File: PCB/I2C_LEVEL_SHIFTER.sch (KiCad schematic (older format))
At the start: 6 parts

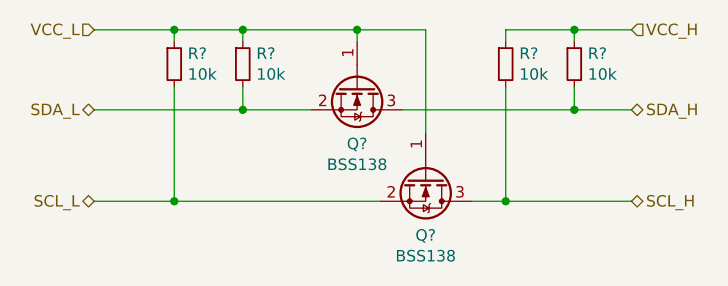
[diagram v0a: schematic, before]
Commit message: Added Humidity and temperature sensors
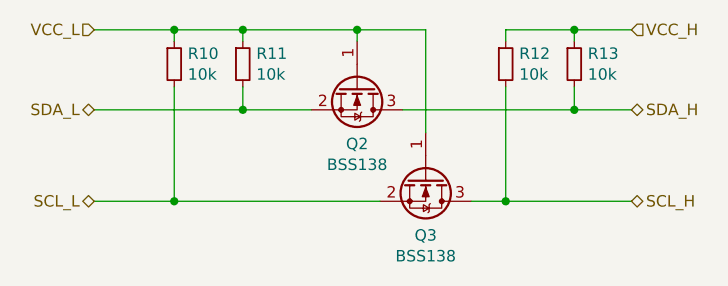
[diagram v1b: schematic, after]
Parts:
- gave numbers to parts that had none: 6
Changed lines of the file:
@@
 $EndDescr
 $Comp
-L Transistor_FET:BSS138 Q?
+L Transistor_FET:BSS138 Q2
 U 1 1 5E8E373A
 P 6100 3750
-F 0 "Q?" V 6349 3750 50  0000 C CNN
+F 0 "Q2" V 6349 3750 50  0000 C CNN
 F 1 "BSS138" V 6440 3750 50  0000 C CNN
 F 2 "Package_TO_SOT_SMD:SOT-23" H 6300 3675 50  0001 L CIN
@@
 $EndComp
 $Comp
-L Transistor_FET:BSS138 Q?
+L Transistor_FET:BSS138 Q3
 U 1 1 5E8E4A70
 P 6400 4150
-F 0 "Q?" V 6649 4150 50  0000 C CNN
+F 0 "Q3" V 6649 4150 50  0000 C CNN
 F 1 "BSS138" V 6740 4150 50  0000 C CNN
 F 2 "Package_TO_SOT_SMD:SOT-23" H 6600 4075 50  0001 L CIN
@@
 	6300 3850 7050 3850
 $Comp
-L Device:R_Small R?
+L Device:R_Small R13
 U 1 1 5E8E9A65
 P 7050 3650
-F 0 "R?" H 7109 3696 50  0000 L CNN
+F 0 "R13" H 7109 3696 50  0000 L CNN
 F 1 "10k" H 7109 3605 50  0000 L CNN
 F 2 "" H 7050 3650 50  0001 C CNN
@@
 $EndComp
 $Comp
-L Device:R_Small R?
+L Device:R_Small R12
 U 1 1 5E8EA22E
 P 6750 3650
-F 0 "R?" H 6809 3696 50  0000 L CNN
+F 0 "R12" H 6809 3696 50  0000 L CNN
 F 1 "10k" H 6809 3605 50  0000 L CNN
 F 2 "" H 6750 3650 50  0001 C CNN
@@
 $EndComp
 $Comp
-L Device:R_Small R?
+L Device:R_Small R11
 U 1 1 5E8EC794
 P 5600 3650
-F 0 "R?" H 5659 3696 50  0000 L CNN
+F 0 "R11" H 5659 3696 50  0000 L CNN
 F 1 "10k" H 5659 3605 50  0000 L CNN
 F 2 "" H 5600 3650 50  0001 C CNN
@@
 $EndComp
 $Comp
-L Device:R_Small R?
+L Device:R_Small R10
 U 1 1 5E8EC79A
 P 5300 3650
-F 0 "R?" H 5359 3696 50  0000 L CNN
+F 0 "R10" H 5359 3696 50  0000 L CNN
 F 1 "10k" H 5359 3605 50  0000 L CNN
 F 2 "" H 5300 3650 50  0001 C CNN

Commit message: Added majority footprints
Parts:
- R10, R11, R12, R13: footprint (none) -> Resistor_SMD:R_0603_1608Metric
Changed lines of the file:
@@
 F 0 "R13" H 7109 3696 50  0000 L CNN
 F 1 "10k" H 7109 3605 50  0000 L CNN
-F 2 "" H 7050 3650 50  0001 C CNN
+F 2 "Resistor_SMD:R_0603_1608Metric" H 7050 3650 50  0001 C CNN
 F 3 "~" H 7050 3650 50  0001 C CNN
 	1    7050 3650
@@
 F 0 "R12" H 6809 3696 50  0000 L CNN
 F 1 "10k" H 6809 3605 50  0000 L CNN
-F 2 "" H 6750 3650 50  0001 C CNN
+F 2 "Resistor_SMD:R_0603_1608Metric" H 6750 3650 50  0001 C CNN
 F 3 "~" H 6750 3650 50  0001 C CNN
 	1    6750 3650
@@
 F 0 "R11" H 5659 3696 50  0000 L CNN
 F 1 "10k" H 5659 3605 50  0000 L CNN
-F 2 "" H 5600 3650 50  0001 C CNN
+F 2 "Resistor_SMD:R_0603_1608Metric" H 5600 3650 50  0001 C CNN
 F 3 "~" H 5600 3650 50  0001 C CNN
 	1    5600 3650
@@
 F 0 "R10" H 5359 3696 50  0000 L CNN
 F 1 "10k" H 5359 3605 50  0000 L CNN
-F 2 "" H 5300 3650 50  0001 C CNN
+F 2 "Resistor_SMD:R_0603_1608Metric" H 5300 3650 50  0001 C CNN
 F 3 "~" H 5300 3650 50  0001 C CNN
 	1    5300 3650
